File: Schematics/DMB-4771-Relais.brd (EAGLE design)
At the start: 50 x 86.9 mm, 21 parts

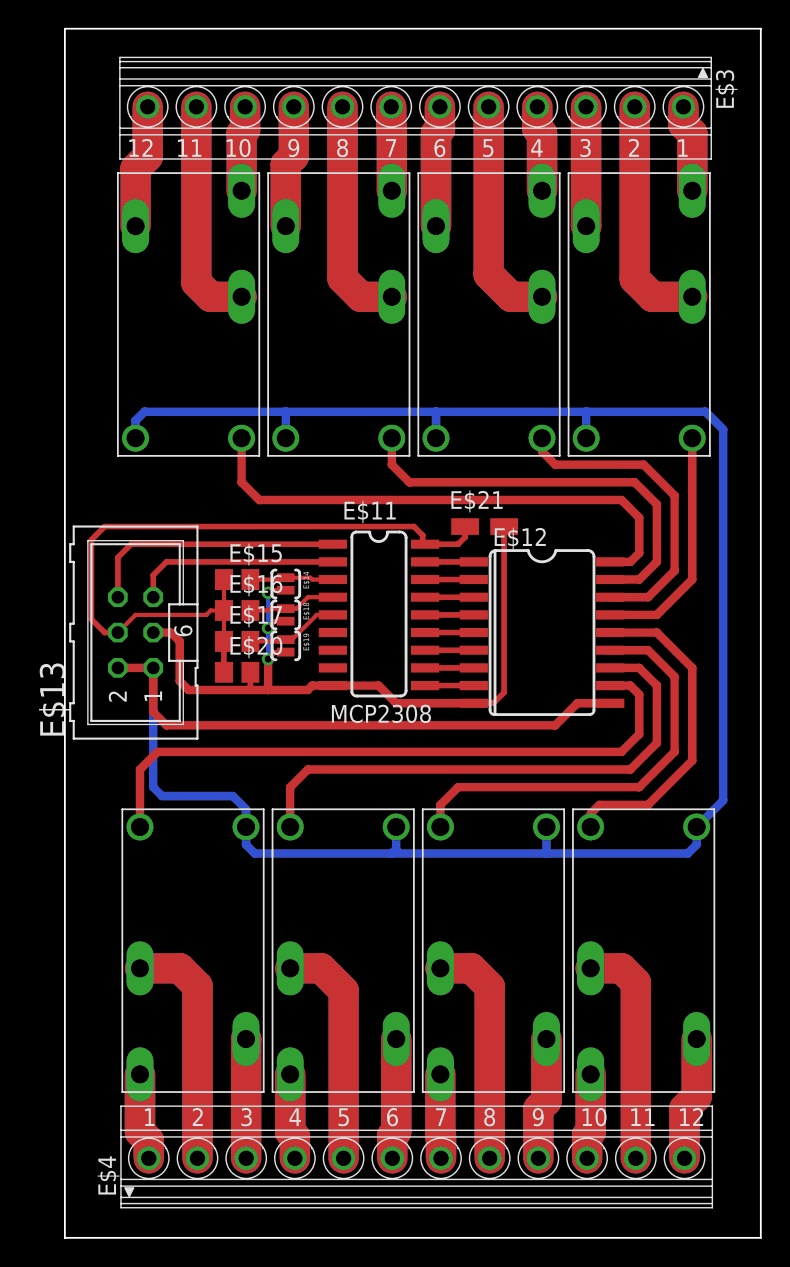
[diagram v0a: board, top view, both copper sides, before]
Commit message: Ajout dip switch bord de carte
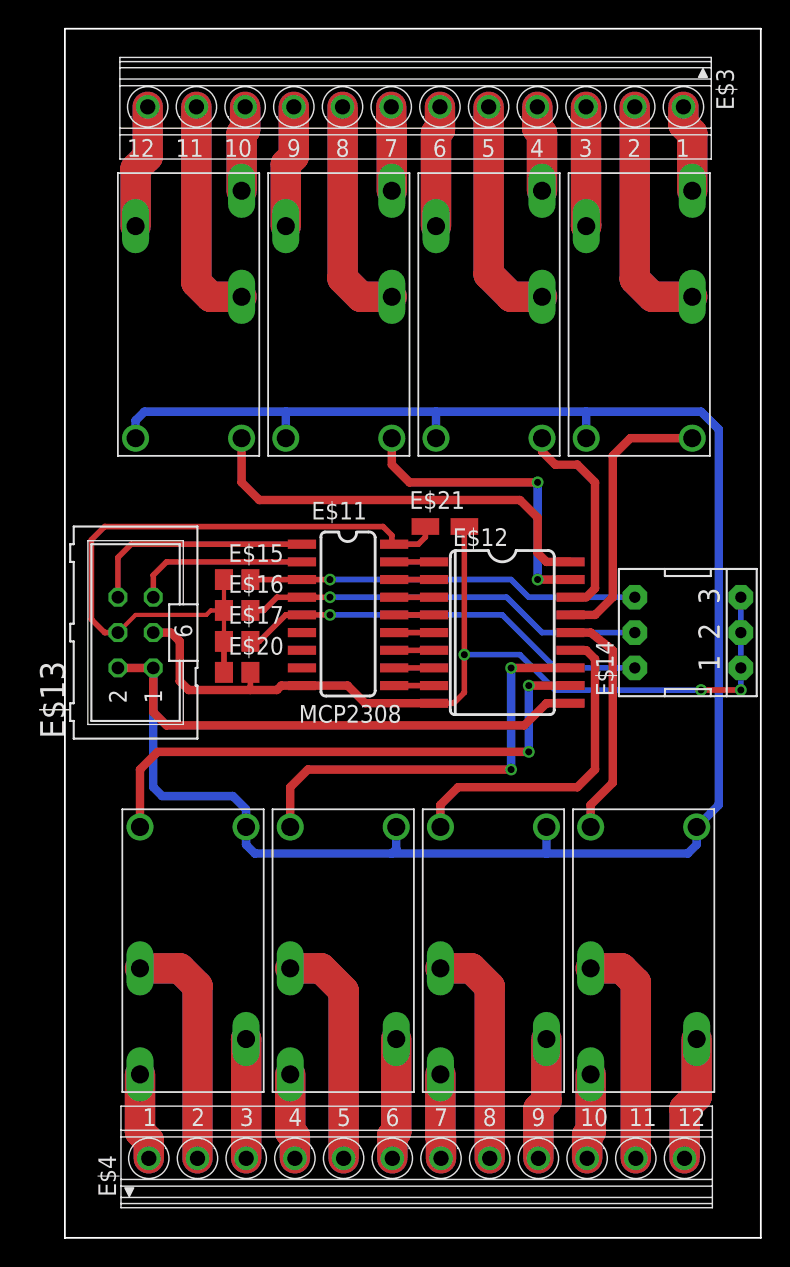
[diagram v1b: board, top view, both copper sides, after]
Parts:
- removed E$18, E$19: (no value), SparkFun-Capacitors:SJ_2S-NO
- E$14: device SparkFun-Capacitors:SJ_2S-NO -> special:EPG-03-SMALL
- moved E$14 29.1 mm to (44.8, 43.5), turned to 90 degrees
- moved E$21 2.86 mm to (27.3, 51.1)
- moved E$12 2.86 mm to (31.4, 47.9)
- moved E$11 2.22 mm to (20.3, 42.2)
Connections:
- removed net S$81: E$11.5, E$17.2, E$19.1
- new net S$78: E$11.3, E$14.4, E$15.2
- net GND: now also E$14.1, E$14.3; no longer E$18.2, E$19.2
- net S$79: now also E$11.4, E$14.5, E$16.2; no longer E$11.3, E$14.1, E$15.2
- net S$80: now also E$11.5, E$14.6, E$17.2; no longer E$11.4, E$16.2, E$18.1
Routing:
- net S$78: track 0.00 -> 28.2 mm, vias 0 -> 1
- net S$80: track 6.32 -> 30.0 mm, vias 0 -> 1
- net S$79: track 6.11 -> 29.1 mm, vias 0 -> 1
- net GND: track 54.1 -> 67.5 mm
- net S$71: track 30.1 -> 22.3 mm, vias 0 -> 2
- net S$76: track 38.5 -> 30.8 mm, vias 0 -> 2
- net S$72: track 22.6 -> 15.3 mm
- net S$75: track 30.8 -> 23.7 mm
- net S$70: track 37.7 -> 30.7 mm
- net S$81: track 6.79 -> 0.00 mm
- net S$74: track 23.4 -> 16.8 mm
- net S$77: track 46.3 -> 40.4 mm, vias 0 -> 2
- net 5V: track 175.5 -> 172.2 mm
- net S$73: track 17.1 -> 20.0 mm
- net 3V3: track 52.0 -> 49.1 mm
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
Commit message: Correction empreinte MCP23008
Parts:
- E$11: device SparkFun-DigitalIC:SOIC-18 -> uln-udn:SO18W
- moved E$17 34.4 mm to (46.0, 35.6), turned to 90 degrees
- moved E$16 32.5 mm to (43.5, 35.6), turned to 90 degrees
- moved E$15 30.9 mm to (41.0, 35.6), turned to 90 degrees
- moved E$20 3.27 mm to (10.8, 43.5), turned to 90 degrees
- moved E$11 3.18 mm to (18.4, 44.8)
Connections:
- net 3V3: now also E$20.2; no longer E$20.1
- net GND: now also E$20.1; no longer E$20.2
- net S$78: now also E$17.2; no longer E$15.2
- net S$80: now also E$15.2; no longer E$17.2
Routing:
- net 3V3: track 49.1 -> 97.5 mm, vias 0 -> 1
- net S$78: track 28.2 -> 41.2 mm
- net S$79: track 29.1 -> 39.4 mm
- net GND: track 67.5 -> 73.0 mm
- net SCL: track 16.5 -> 12.8 mm
- net SDA: track 12.7 -> 9.02 mm
- net S$80: track 30.0 -> 33.6 mm
